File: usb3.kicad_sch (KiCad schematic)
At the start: 44 parts, among them J1 USB3_A, J17 Conn_01x15_MountingPin, J4 USB4105-GF-A, Q3 BSS138, U22 TPD4E05U06QDQARQ1, U23 TPD4E05U06QDQARQ1, U27 AP22615A, U28 TPD4E05U06QDQARQ1, U30 AP22615A, U34 TPD4E05U06QDQARQ1, U35 TPD4E05U06QDQARQ1

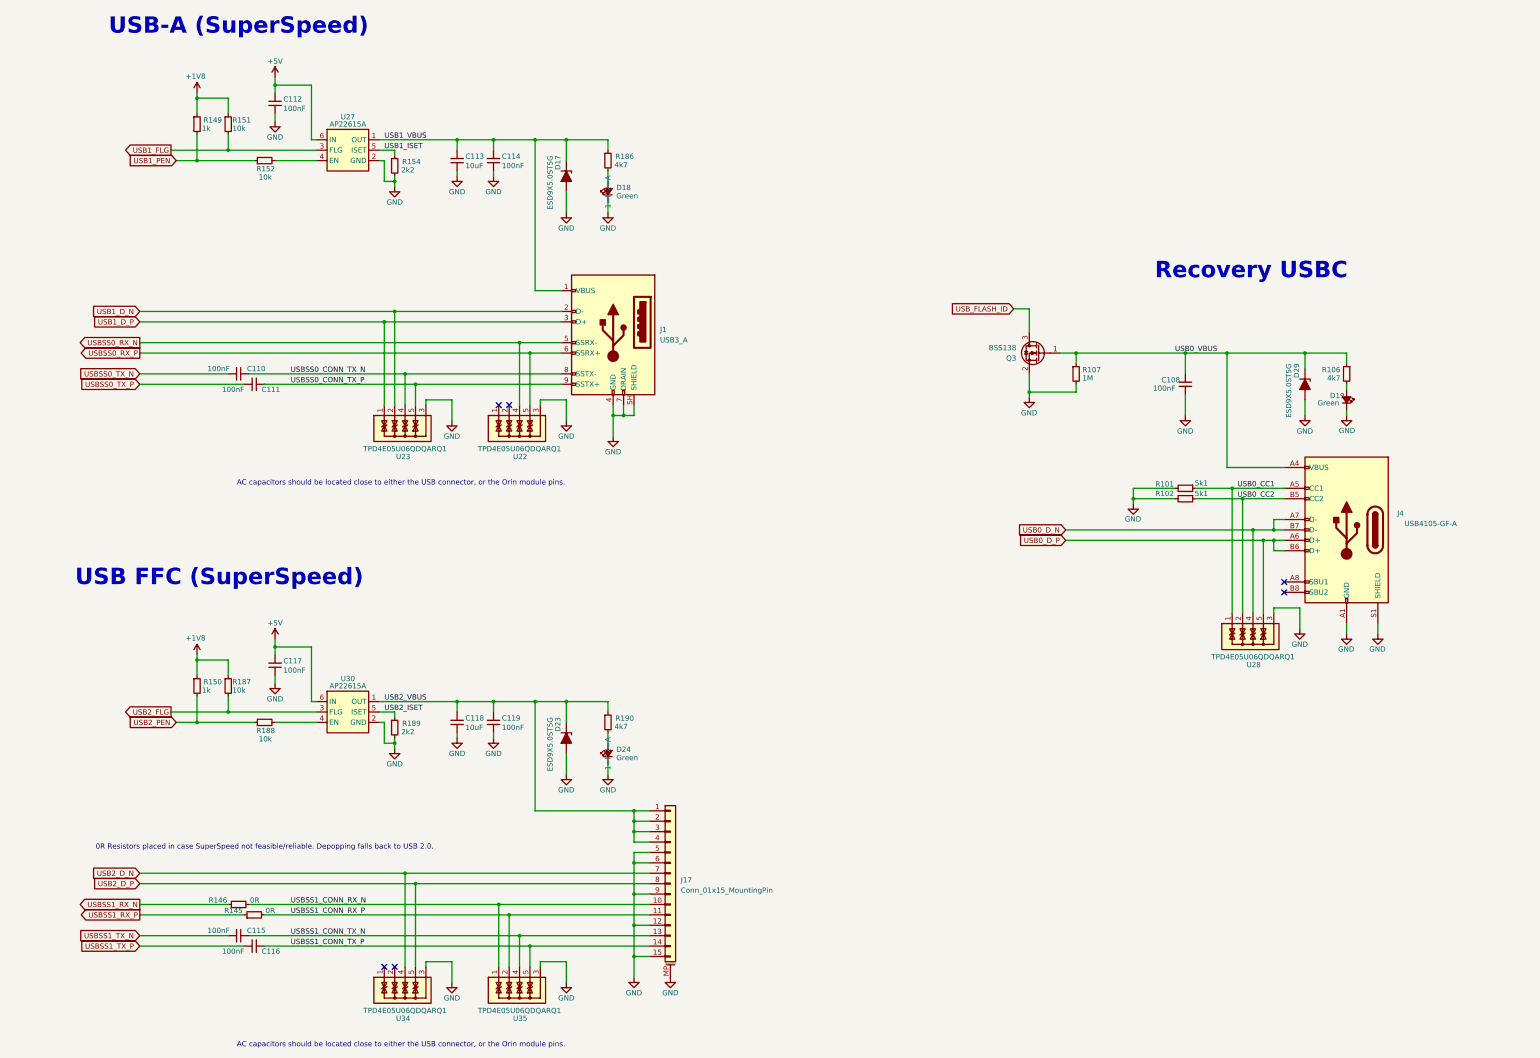
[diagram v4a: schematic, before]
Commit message: route all diff pairs, length tuning
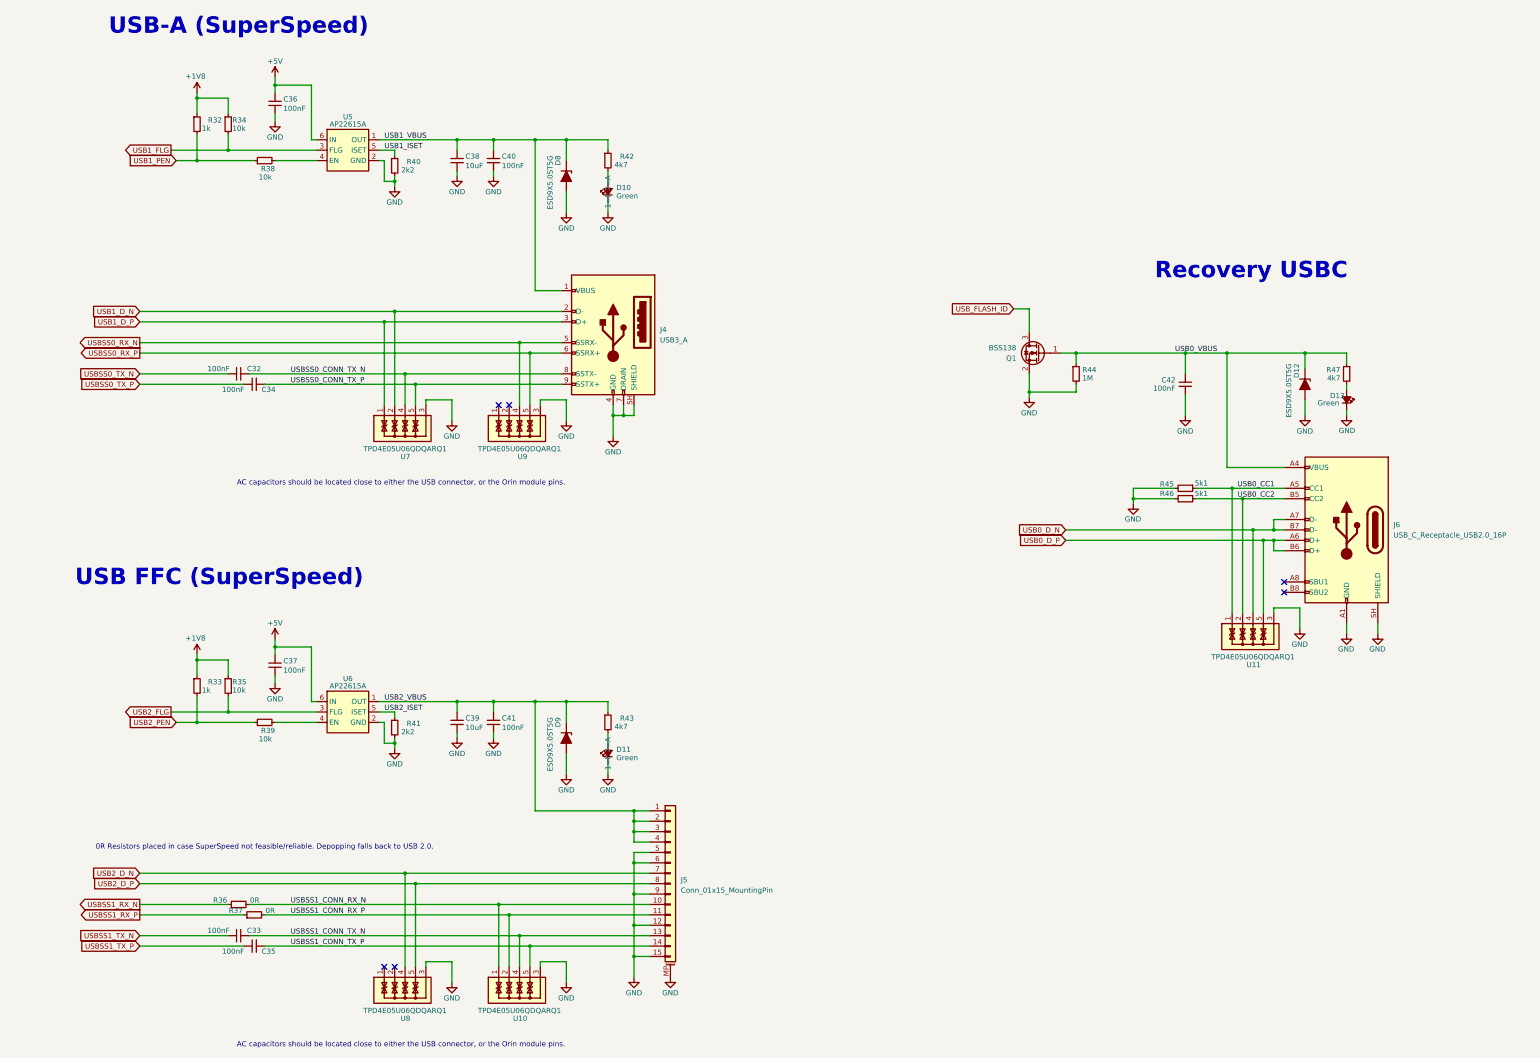
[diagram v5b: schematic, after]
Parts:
- removed J4: USB4105-GF-A, Connector_USB:USB_C_Receptacle_GCT_USB4105-xx-A_16P_TopMnt_Horizontal, symbol Connector:USB_C_Receptacle_USB2.0_16P
- added J6: USB_C_Receptacle_USB2.0_16P, Connector_USB:USB_C_Receptacle_GCT_USB4105-xx-A_16P_TopMnt_Horizontal, symbol Connector:USB_C_Receptacle_USB2.0_16P
- R45: renamed from R101; footprint Resistor_SMD:R_0402_1005Metric -> Resistor_SMD:R_0603_1608Metric
- R46: renamed from R102; footprint Resistor_SMD:R_0402_1005Metric -> Resistor_SMD:R_0603_1608Metric
- renumbered C110 to C32, C115 to C33, C111 to C34, C116 to C35, C112 to C36, C117 to C37, C113 to C38, C118 to C39, C114 to C40, C119 to C41, C108 to C42, D18 to D10, D24 to D11, D29 to D12, D19 to D13, D17 to D8, D23 to D9, J1 to J4, J17 to J5, Q3 to Q1, R149 to R32, R150 to R33, R151 to R34, R187 to R35, R146 to R36, R145 to R37, R152 to R38, R188 to R39, R154 to R40, R189 to R41, R186 to R42, R190 to R43, R107 to R44, R106 to R47, U35 to U10, U28 to U11, U27 to U5, U30 to U6, U23 to U7, U34 to U8, U22 to U9
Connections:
- net GND: now also J6.A1 (GND), J6.A12 (GND), J6.B1 (GND), J6.B12 (GND), J6.SH (SHIELD)
- net USB0_CC1: now also J6.A5 (CC1)
- net USB0_CC2: now also J6.B5 (CC2)
- net USB0_D_N: now also J6.A7 (D-), J6.B7 (D-)
- net USB0_D_P: now also J6.A6 (D+), J6.B6 (D+)
- net USB0_VBUS: now also J6.A4 (VBUS), J6.A9 (VBUS), J6.B4 (VBUS), J6.B9 (VBUS)
